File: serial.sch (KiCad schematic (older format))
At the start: 53 parts, among them CN304 Conn_02x13_Odd_Even, CN305 DB25P, CN306 Conn_01x03_Male, Q300 2SC945, Q302 2N3906, U1 PST518B, U301 8520, U302 74LS32, U303 74F08, U304 1488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

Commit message: Associate footprints with components
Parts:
- CN304: footprint (none) -> Connector_PinSocket_2.54mm:PinSocket_2x13_P2.54mm_Vertical
- CN305: footprint (none) -> Connector_Dsub:DSUB-25_Male_Horizontal_P2.77x2.84mm_EdgePinOffset7.70mm_Housed_MountingHolesOffset9.12mm
- CN306, EMI325, EMI326, EMI327, EMI328, EMI329, EMI330, EMI331, EMI332, EMI333, EMI334: footprint (none) -> Connector_PinSocket_2.54mm:PinSocket_1x03_P2.54mm_Vertical
- F2: footprint (none) -> Fuse:Fuse_Littelfuse-LVR100
- Q300: footprint (none) -> Package_TO_SOT_THT:TO-92_Inline
- R302, R305, R306, R307, R308, R802, R805, R902: footprint (none) -> Resistor_THT:R_Axial_DIN0207_L6.3mm_D2.5mm_P10.16mm_Horizontal
- U1: footprint (none) -> Package_TO_SOT_THT:TO-92L_Inline
- U301: footprint (none) -> Package_DIP:DIP-40_W15.24mm_Socket
- U302, U303, U304, U305, U805: footprint (none) -> Package_DIP:DIP-14_W7.62mm_Socket
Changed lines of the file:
@@
 F 0 "U301" H 2800 4565 50  0000 C CNN
 F 1 "8520" H 2800 4474 50  0000 C CNN
-F 2 "" H 4400 4350 50  0001 C CNN
+F 2 "Package_DIP:DIP-40_W15.24mm_Socket" H 4400 4350 50  0001 C CNN
 F 3 "https://www.amigawiki.org/doku.php?id=de:parts:cia" H 4400 4350 50  0001 C CNN
 	1    2800 4400
@@
 F 0 "U302" H 1650 6183 50  0000 C CNN
 F 1 "74LS32" H 1650 6274 50  0000 C CNN
-F 2 "" H 1650 6500 50  0001 C CNN
+F 2 "Package_DIP:DIP-14_W7.62mm_Socket" H 1650 6500 50  0001 C CNN
 F 3 "http://www.ti.com/lit/gpn/sn74LS32" H 1650 6500 50  0001 C CNN
 	2    1650 6500
@@
 F 0 "U805" H 2150 1083 50  0000 C CNN
 F 1 "LM339" H 2150 1174 50  0000 C CNN
-F 2 "" H 2100 1550 50  0001 C CNN
+F 2 "Package_DIP:DIP-14_W7.62mm_Socket" H 2100 1550 50  0001 C CNN
 F 3 "http://www.ti.com/lit/ds/symlink/lm339.pdf" H 2200 1650 50  0001 C CNN
 	2    2150 1450
@@
 F 0 "R802" H 2670 1246 50  0000 L CNN
 F 1 "10k" H 2670 1155 50  0000 L CNN
-F 2 "" V 2530 1200 50  0001 C CNN
+F 2 "Resistor_THT:R_Axial_DIN0207_L6.3mm_D2.5mm_P10.16mm_Horizontal" V 2530 1200 50  0001 C CNN
 F 3 "~" H 2600 1200 50  0001 C CNN
 	1    2600 1200
@@
 F 0 "U805" H 3800 1183 50  0000 C CNN
 F 1 "LM339" H 3800 1274 50  0000 C CNN
-F 2 "" H 3750 1650 50  0001 C CNN
+F 2 "Package_DIP:DIP-14_W7.62mm_Socket" H 3750 1650 50  0001 C CNN
 F 3 "http://www.ti.com/lit/ds/symlink/lm339.pdf" H 3850 1750 50  0001 C CNN
 	1    3800 1550
@@
 F 0 "U805" H 5250 1283 50  0000 C CNN
 F 1 "LM339" H 5250 1374 50  0000 C CNN
-F 2 "" H 5200 1750 50  0001 C CNN
+F 2 "Package_DIP:DIP-14_W7.62mm_Socket" H 5200 1750 50  0001 C CNN
 F 3 "http://www.ti.com/lit/ds/symlink/lm339.pdf" H 5300 1850 50  0001 C CNN
 	3    5250 1650
@@
 F 0 "U805" H 6700 1383 50  0000 C CNN
 F 1 "LM339" H 6700 1474 50  0000 C CNN
-F 2 "" H 6650 1850 50  0001 C CNN
+F 2 "Package_DIP:DIP-14_W7.62mm_Socket" H 6650 1850 50  0001 C CNN
 F 3 "http://www.ti.com/lit/ds/symlink/lm339.pdf" H 6750 1950 50  0001 C CNN
 	4    6700 1750
@@
 F 0 "U805" H 762 2254 50  0000 R CNN
 F 1 "LM339" H 762 2345 50  0000 R CNN
-F 2 "" H 900 2400 50  0001 C CNN
+F 2 "Package_DIP:DIP-14_W7.62mm_Socket" H 900 2400 50  0001 C CNN
 F 3 "http://www.ti.com/lit/ds/symlink/lm339.pdf" H 1000 2500 50  0001 C CNN
 	5    950  2300
@@
 F 0 "R805" H 4320 1446 50  0000 L CNN
 F 1 "47k" H 4320 1355 50  0000 L CNN
-F 2 "" V 4180 1400 50  0001 C CNN
+F 2 "Resistor_THT:R_Axial_DIN0207_L6.3mm_D2.5mm_P10.16mm_Horizontal" V 4180 1400 50  0001 C CNN
 F 3 "~" H 4250 1400 50  0001 C CNN
 	1    4250 1400
@@
 F 0 "CN305" H 14830 6696 50  0000 L CNN
 F 1 "DB25P" H 14830 6605 50  0000 L CNN
-F 2 "" H 14650 6650 50  0001 C CNN
+F 2 "Connector_Dsub:DSUB-25_Male_Horizontal_P2.77x2.84mm_EdgePinOffset7.70mm_Housed_MountingHolesOffset9.12mm" H 14650 6650 50  0001 C CNN
 F 3 " ~" H 14650 6650 50  0001 C CNN
 F 4 "Male" H 14650 6650 50  0001 C CNN "Gender"
@@
 F 0 "R307" H 8770 2746 50  0000 L CNN
 F 1 "68" H 8770 2655 50  0000 L CNN
-F 2 "" V 8630 2700 50  0001 C CNN
+F 2 "Resistor_THT:R_Axial_DIN0207_L6.3mm_D2.5mm_P10.16mm_Horizontal" V 8630 2700 50  0001 C CNN
 F 3 "~" H 8700 2700 50  0001 C CNN
 	1    8700 2700
@@
 F 0 "R902" H 7920 2696 50  0000 L CNN
 F 1 "4.7k" H 7920 2605 50  0000 L CNN
-F 2 "" V 7780 2650 50  0001 C CNN
+F 2 "Resistor_THT:R_Axial_DIN0207_L6.3mm_D2.5mm_P10.16mm_Horizontal" V 7780 2650 50  0001 C CNN
 F 3 "~" H 7850 2650 50  0001 C CNN
 	1    7850 2650
@@
 F 0 "CN306" H 10272 2678 50  0000 R CNN
 F 1 "Conn_01x03_Male" H 10408 2890 50  0001 C CNN
-F 2 "" H 10300 2700 50  0001 C CNN
+F 2 "Connector_PinSocket_2.54mm:PinSocket_1x03_P2.54mm_Vertical" H 10300 2700 50  0001 C CNN
 F 3 "~" H 10300 2700 50  0001 C CNN
 	1    10300 2700
@@
 F 0 "CN304" V 11100 3512 50  0000 R CNN
 F 1 "Conn_02x13_Odd_Even" V 11055 3512 50  0001 R CNN
-F 2 "" H 11050 4200 50  0001 C CNN
+F 2 "Connector_PinSocket_2.54mm:PinSocket_2x13_P2.54mm_Vertical" H 11050 4200 50  0001 C CNN
 F 3 "~" H 11050 4200 50  0001 C CNN
 F 4 "Male" V 11050 4200 50  0001 C CNN "Gender"
@@
 F 0 "U303" H 6250 3775 50  0000 C CNN
 F 1 "74F08" H 6250 3684 50  0000 C CNN
-F 2 "" H 6250 3450 50  0001 C CNN
+F 2 "Package_DIP:DIP-14_W7.62mm_Socket" H 6250 3450 50  0001 C CNN
 F 3 "http://www.ti.com/lit/gpn/sn74LS08" H 6250 3450 50  0001 C CNN
 	2    6250 3450
@@
 F 0 "EMI326" H 11600 5663 50  0000 C CNN
 F 1 "C_Feedthrough" H 11600 5664 50  0001 C CNN
-F 2 "" V 11600 5450 50  0001 C CNN
+F 2 "Connector_PinSocket_2.54mm:PinSocket_1x03_P2.54mm_Vertical" V 11600 5450 50  0001 C CNN
 F 3 "~" V 11600 5450 50  0001 C CNN
 	1    11600 5450
@@
 F 0 "EMI327" H 11600 6063 50  0000 C CNN
 F 1 "C_Feedthrough" H 11600 6064 50  0001 C CNN
-F 2 "" V 11600 5850 50  0001 C CNN
+F 2 "Connector_PinSocket_2.54mm:PinSocket_1x03_P2.54mm_Vertical" V 11600 5850 50  0001 C CNN
 F 3 "~" V 11600 5850 50  0001 C CNN
 	1    11600 5850
@@
 F 0 "EMI330" H 11600 7513 50  0000 C CNN
 F 1 "C_Feedthrough" H 11600 7514 50  0001 C CNN
-F 2 "" V 11600 7300 50  0001 C CNN
+F 2 "Connector_PinSocket_2.54mm:PinSocket_1x03_P2.54mm_Vertical" V 11600 7300 50  0001 C CNN
 F 3 "~" V 11600 7300 50  0001 C CNN
 	1    11600 7300
@@
 F 0 "EMI334" H 15200 8613 50  0000 C CNN
 F 1 "C_Feedthrough" H 15200 8614 50  0001 C CNN
-F 2 "" V 15200 8400 50  0001 C CNN
+F 2 "Connector_PinSocket_2.54mm:PinSocket_1x03_P2.54mm_Vertical" V 15200 8400 50  0001 C CNN
 F 3 "~" V 15200 8400 50  0001 C CNN
 	1    15200 8400
@@
 F 0 "EMI333" H 12950 8713 50  0000 C CNN
 F 1 "C_Feedthrough" H 12950 8714 50  0001 C CNN
-F 2 "" V 12950 8500 50  0001 C CNN
+F 2 "Connector_PinSocket_2.54mm:PinSocket_1x03_P2.54mm_Vertical" V 12950 8500 50  0001 C CNN
 F 3 "~" V 12950 8500 50  0001 C CNN
 	1    12950 8500
@@
 F 0 "EMI332" H 14600 8613 50  0000 C CNN
 F 1 "C_Feedthrough" H 14600 8614 50  0001 C CNN
-F 2 "" V 14600 8400 50  0001 C CNN
+F 2 "Connector_PinSocket_2.54mm:PinSocket_1x03_P2.54mm_Vertical" V 14600 8400 50  0001 C CNN
 F 3 "~" V 14600 8400 50  0001 C CNN
 	1    14600 8400
@@
 F 0 "EMI331" H 11600 8063 50  0000 C CNN
 F 1 "C_Feedthrough" H 11600 8064 50  0001 C CNN
-F 2 "" V 11600 7850 50  0001 C CNN
+F 2 "Connector_PinSocket_2.54mm:PinSocket_1x03_P2.54mm_Vertical" V 11600 7850 50  0001 C CNN
 F 3 "~" V 11600 7850 50  0001 C CNN
 	1    11600 7850
@@
 F 0 "EMI325" H 11600 5263 50  0000 C CNN
 F 1 "C_Feedthrough" H 11600 5264 50  0001 C CNN
-F 2 "" V 11600 5050 50  0001 C CNN
+F 2 "Connector_PinSocket_2.54mm:PinSocket_1x03_P2.54mm_Vertical" V 11600 5050 50  0001 C CNN
 F 3 "~" V 11600 5050 50  0001 C CNN
 	1    11600 5050
@@
 F 0 "EMI329" H 11600 7113 50  0000 C CNN
 F 1 "C_Feedthrough" H 11600 7114 50  0001 C CNN
-F 2 "" V 11600 6900 50  0001 C CNN
+F 2 "Connector_PinSocket_2.54mm:PinSocket_1x03_P2.54mm_Vertical" V 11600 6900 50  0001 C CNN
 F 3 "~" V 11600 6900 50  0001 C CNN
 	1    11600 6900
@@
 F 0 "EMI328" H 11600 6713 50  0000 C CNN
 F 1 "C_Feedthrough" H 11600 6714 50  0001 C CNN
-F 2 "" V 11600 6500 50  0001 C CNN
+F 2 "Connector_PinSocket_2.54mm:PinSocket_1x03_P2.54mm_Vertical" V 11600 6500 50  0001 C CNN
 F 3 "~" V 11600 6500 50  0001 C CNN
 	1    11600 6500
@@
 F 0 "R308" H 9220 2496 50  0000 L CNN
 F 1 "200" H 9220 2405 50  0000 L CNN
-F 2 "" V 9080 2450 50  0001 C CNN
+F 2 "Resistor_THT:R_Axial_DIN0207_L6.3mm_D2.5mm_P10.16mm_Horizontal" V 9080 2450 50  0001 C CNN
 F 3 "~" H 9150 2450 50  0001 C CNN
 	1    9150 2450
@@
 F 0 "U304" H 6450 4525 50  0000 C CNN
 F 1 "1488" H 6450 4434 50  0000 C CNN
-F 2 "" H 6450 4500 50  0001 C CNN
+F 2 "Package_DIP:DIP-14_W7.62mm_Socket" H 6450 4500 50  0001 C CNN
 F 3 "https://www.onsemi.com/pub/Collateral/MC1488-D.PDF" H 6450 4500 50  0001 C CNN
 	1    6450 4500
@@
 F 0 "U305" H 6450 6225 50  0000 C CNN
 F 1 "1489" H 6450 6134 50  0000 C CNN
-F 2 "" H 6450 6200 50  0001 C CNN
+F 2 "Package_DIP:DIP-14_W7.62mm_Socket" H 6450 6200 50  0001 C CNN
 F 3 "https://www.onsemi.com/pub/Collateral/MC1489-D.PDF" H 6450 6200 50  0001 C CNN
 	1    6450 6200
@@
 F 0 "Q300" H 10641 8846 50  0000 L CNN
 F 1 "2SC945" H 10641 8755 50  0000 L CNN
-F 2 "" H 10650 8900 50  0001 C CNN
+F 2 "Package_TO_SOT_THT:TO-92_Inline" H 10650 8900 50  0001 C CNN
 F 3 "~" H 10450 8800 50  0001 C CNN
 	1    10450 8800
@@
 F 0 "R305" H 10970 9096 50  0000 L CNN
 F 1 "10k" H 10970 9005 50  0000 L CNN
-F 2 "" V 10830 9050 50  0001 C CNN
+F 2 "Resistor_THT:R_Axial_DIN0207_L6.3mm_D2.5mm_P10.16mm_Horizontal" V 10830 9050 50  0001 C CNN
 F 3 "~" H 10900 9050 50  0001 C CNN
 	1    10900 9050
@@
 F 0 "R306" H 11420 8596 50  0000 L CNN
 F 1 "10k" H 11420 8505 50  0000 L CNN
-F 2 "" V 11280 8550 50  0001 C CNN
+F 2 "Resistor_THT:R_Axial_DIN0207_L6.3mm_D2.5mm_P10.16mm_Horizontal" V 11280 8550 50  0001 C CNN
 F 3 "~" H 11350 8550 50  0001 C CNN
 	1    11350 8550
@@
 F 0 "R302" V 13193 9050 50  0000 C CNN
 F 1 "1k" V 13284 9050 50  0000 C CNN
-F 2 "" V 13330 9050 50  0001 C CNN
+F 2 "Resistor_THT:R_Axial_DIN0207_L6.3mm_D2.5mm_P10.16mm_Horizontal" V 13330 9050 50  0001 C CNN
 F 3 "~" H 13400 9050 50  0001 C CNN
 	1    13400 9050
@@
 F 0 "F2" H 14910 8900 50  0000 L CNN
 F 1 "Fuse" H 14910 8855 50  0001 L CNN
-F 2 "" V 14780 8900 50  0001 C CNN
+F 2 "Fuse:Fuse_Littelfuse-LVR100" V 14780 8900 50  0001 C CNN
 F 3 "~" H 14850 8900 50  0001 C CNN
 	1    14850 8900
@@
 F 0 "U1" H 3475 765 50  0000 C CNN
 F 1 "PST518B" H 3475 674 50  0000 C CNN
-F 2 "" H 3400 650 50  0001 C CNN
+F 2 "Package_TO_SOT_THT:TO-92L_Inline" H 3400 650 50  0001 C CNN
 F 3 "http://www.amigawiki.org/lib/exe/fetch.php?media=de:service:upgrades:pst518b_mitsumi_datasheet.pdf" H 3400 650 50  0001 C CNN
 	1    3400 650

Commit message: Associate more components
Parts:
- C317, C318, C813, C814: footprint (none) -> Capacitor_THT:CP_Radial_D8.0mm_P5.00mm
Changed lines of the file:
@@
 F 0 "C813" H 2718 1746 50  0000 L CNN
 F 1 "22uF 16V" H 2718 1655 50  0000 L CNN
-F 2 "" H 2638 1550 50  0001 C CNN
+F 2 "Capacitor_THT:CP_Radial_D8.0mm_P5.00mm" H 2638 1550 50  0001 C CNN
 F 3 "~" H 2600 1700 50  0001 C CNN
 	1    2600 1700
@@
 F 0 "C814" H 4368 1746 50  0000 L CNN
 F 1 "22uF 16V" H 4368 1655 50  0000 L CNN
-F 2 "" H 4288 1550 50  0001 C CNN
+F 2 "Capacitor_THT:CP_Radial_D8.0mm_P5.00mm" H 4288 1550 50  0001 C CNN
 F 3 "~" H 4250 1700 50  0001 C CNN
 	1    4250 1700
@@
 F 0 "C318" H 12668 8946 50  0000 L CNN
 F 1 "22uF 16V" H 12668 8855 50  0000 L CNN
-F 2 "" H 12588 8750 50  0001 C CNN
+F 2 "Capacitor_THT:CP_Radial_D8.0mm_P5.00mm" H 12588 8750 50  0001 C CNN
 F 3 "~" H 12550 8900 50  0001 C CNN
 	1    12550 8900
@@
 F 0 "C317" H 13268 4996 50  0000 L CNN
 F 1 "22uF 16V" H 13268 4905 50  0000 L CNN
-F 2 "" H 13188 4800 50  0001 C CNN
+F 2 "Capacitor_THT:CP_Radial_D8.0mm_P5.00mm" H 13188 4800 50  0001 C CNN
 F 3 "~" H 13150 4950 50  0001 C CNN
 	1    13150 4950

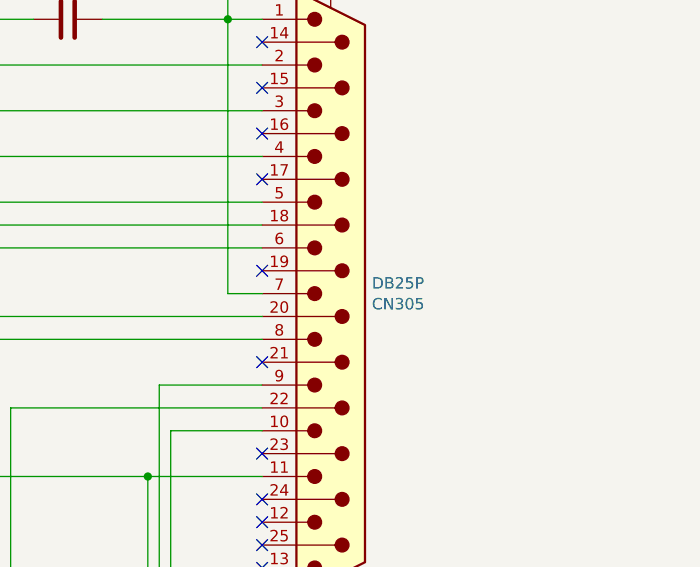
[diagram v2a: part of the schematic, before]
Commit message: Change namings
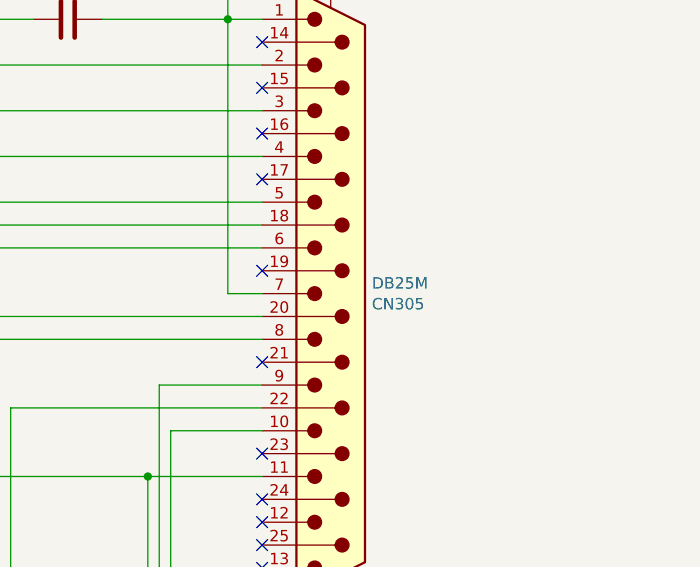
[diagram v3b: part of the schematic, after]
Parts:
- CN305: value DB25P -> DB25M
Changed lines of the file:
@@
 P 14650 6650
 F 0 "CN305" H 14830 6696 50  0000 L CNN
-F 1 "DB25P" H 14830 6605 50  0000 L CNN
+F 1 "DB25M" H 14830 6605 50  0000 L CNN
 F 2 "Connector_Dsub:DSUB-25_Male_Horizontal_P2.77x2.84mm_EdgePinOffset7.70mm_Housed_MountingHolesOffset9.12mm" H 14650 6650 50  0001 C CNN
 F 3 " ~" H 14650 6650 50  0001 C CNN

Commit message: Update footprints
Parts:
- C301, C304, C305, C306, C310, C311, C312, C313, C314, C315, C316, C320, C321, C805, C815, C919: footprint (none) -> Capacitor_THT:C_Rect_L11.0mm_W2.8mm_P10.00mm_MKT
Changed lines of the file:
@@
 F 0 "C301" H 1715 4496 50  0000 L CNN
 F 1 "0.1uF" H 1715 4405 50  0000 L CNN
-F 2 "" H 1638 4300 50  0001 C CNN
+F 2 "Capacitor_THT:C_Rect_L11.0mm_W2.8mm_P10.00mm_MKT" H 1638 4300 50  0001 C CNN
 F 3 "~" H 1600 4450 50  0001 C CNN
 	1    1600 4450
@@
 F 0 "C805" H 1165 2346 50  0000 L CNN
 F 1 "0.1uF" H 1165 2255 50  0000 L CNN
-F 2 "" H 1088 2150 50  0001 C CNN
+F 2 "Capacitor_THT:C_Rect_L11.0mm_W2.8mm_P10.00mm_MKT" H 1088 2150 50  0001 C CNN
 F 3 "~" H 1050 2300 50  0001 C CNN
 	1    1050 2300
@@
 F 0 "C815" H 4165 2296 50  0000 L CNN
 F 1 "0.1uF" H 4165 2205 50  0000 L CNN
-F 2 "" H 4088 2100 50  0001 C CNN
+F 2 "Capacitor_THT:C_Rect_L11.0mm_W2.8mm_P10.00mm_MKT" H 4088 2100 50  0001 C CNN
 F 3 "~" H 4050 2250 50  0001 C CNN
 	1    4050 2250
@@
 F 0 "C320" H 10115 4196 50  0000 L CNN
 F 1 "470pF" H 10115 4105 50  0000 L CNN
-F 2 "" H 10038 4000 50  0001 C CNN
+F 2 "Capacitor_THT:C_Rect_L11.0mm_W2.8mm_P10.00mm_MKT" H 10038 4000 50  0001 C CNN
 F 3 "~" H 10000 4150 50  0001 C CNN
 	1    10000 4150
@@
 F 0 "C321" V 11348 3350 50  0000 C CNN
 F 1 "470pF" V 11439 3350 50  0000 C CNN
-F 2 "" H 11638 3200 50  0001 C CNN
+F 2 "Capacitor_THT:C_Rect_L11.0mm_W2.8mm_P10.00mm_MKT" H 11638 3200 50  0001 C CNN
 F 3 "~" H 11600 3350 50  0001 C CNN
 	1    11600 3350
@@
 F 0 "C919" H 9265 2996 50  0000 L CNN
 F 1 "0.1uF" H 9265 2905 50  0000 L CNN
-F 2 "" H 9188 2800 50  0001 C CNN
+F 2 "Capacitor_THT:C_Rect_L11.0mm_W2.8mm_P10.00mm_MKT" H 9188 2800 50  0001 C CNN
 F 3 "~" H 9150 2950 50  0001 C CNN
 	1    9150 2950
@@
 F 0 "C305" V 6198 7850 50  0000 C CNN
 F 1 "0.01uF" V 6289 7850 50  0000 C CNN
-F 2 "" H 6488 7700 50  0001 C CNN
+F 2 "Capacitor_THT:C_Rect_L11.0mm_W2.8mm_P10.00mm_MKT" H 6488 7700 50  0001 C CNN
 F 3 "~" H 6450 7850 50  0001 C CNN
 	1    6450 7850
@@
 F 0 "C314" H 7565 4346 50  0000 L CNN
 F 1 "1000pF" H 7565 4255 50  0000 L CNN
-F 2 "" H 7488 4150 50  0001 C CNN
+F 2 "Capacitor_THT:C_Rect_L11.0mm_W2.8mm_P10.00mm_MKT" H 7488 4150 50  0001 C CNN
 F 3 "~" H 7450 4300 50  0001 C CNN
 	1    7450 4300
@@
 F 0 "C315" H 8015 4646 50  0000 L CNN
 F 1 "1000pF" H 8015 4555 50  0000 L CNN
-F 2 "" H 7938 4450 50  0001 C CNN
+F 2 "Capacitor_THT:C_Rect_L11.0mm_W2.8mm_P10.00mm_MKT" H 7938 4450 50  0001 C CNN
 F 3 "~" H 7900 4600 50  0001 C CNN
 	1    7900 4600
@@
 F 0 "C316" H 8415 4346 50  0000 L CNN
 F 1 "1000pF" H 8415 4255 50  0000 L CNN
-F 2 "" H 8338 4150 50  0001 C CNN
+F 2 "Capacitor_THT:C_Rect_L11.0mm_W2.8mm_P10.00mm_MKT" H 8338 4150 50  0001 C CNN
 F 3 "~" H 8300 4300 50  0001 C CNN
 	1    8300 4300
@@
 F 0 "C310" H 7615 8146 50  0000 L CNN
 F 1 "1000pF" H 7615 8055 50  0000 L CNN
-F 2 "" H 7538 7950 50  0001 C CNN
+F 2 "Capacitor_THT:C_Rect_L11.0mm_W2.8mm_P10.00mm_MKT" H 7538 7950 50  0001 C CNN
 F 3 "~" H 7500 8100 50  0001 C CNN
 	1    7500 8100
@@
 F 0 "C311" H 8115 8146 50  0000 L CNN
 F 1 "1000pF" H 8115 8055 50  0000 L CNN
-F 2 "" H 8038 7950 50  0001 C CNN
+F 2 "Capacitor_THT:C_Rect_L11.0mm_W2.8mm_P10.00mm_MKT" H 8038 7950 50  0001 C CNN
 F 3 "~" H 8000 8100 50  0001 C CNN
 	1    8000 8100
@@
 F 0 "C312" H 8615 8146 50  0000 L CNN
 F 1 "1000pF" H 8615 8055 50  0000 L CNN
-F 2 "" H 8538 7950 50  0001 C CNN
+F 2 "Capacitor_THT:C_Rect_L11.0mm_W2.8mm_P10.00mm_MKT" H 8538 7950 50  0001 C CNN
 F 3 "~" H 8500 8100 50  0001 C CNN
 	1    8500 8100
@@
 F 0 "C313" H 9115 8146 50  0000 L CNN
 F 1 "1000pF" H 9115 8055 50  0000 L CNN
-F 2 "" H 9038 7950 50  0001 C CNN
+F 2 "Capacitor_THT:C_Rect_L11.0mm_W2.8mm_P10.00mm_MKT" H 9038 7950 50  0001 C CNN
 F 3 "~" H 9000 8100 50  0001 C CNN
 	1    9000 8100
@@
 F 0 "C304" H 13965 8396 50  0000 L CNN
 F 1 "100pF" H 13965 8305 50  0000 L CNN
-F 2 "" H 13888 8200 50  0001 C CNN
+F 2 "Capacitor_THT:C_Rect_L11.0mm_W2.8mm_P10.00mm_MKT" H 13888 8200 50  0001 C CNN
 F 3 "~" H 13850 8350 50  0001 C CNN
 	1    13850 8350
@@
 F 0 "C306" V 13248 5450 50  0000 C CNN
 F 1 "100pF" V 13339 5450 50  0000 C CNN
-F 2 "" H 13538 5300 50  0001 C CNN
+F 2 "Capacitor_THT:C_Rect_L11.0mm_W2.8mm_P10.00mm_MKT" H 13538 5300 50  0001 C CNN
 F 3 "~" H 13500 5450 50  0001 C CNN
 	1    13500 5450

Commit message: More placement
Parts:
- CN304: footprint Connector_PinSocket_2.54mm:PinSocket_2x13_P2.54mm_Vertical -> Connector_PinHeader_2.54mm:PinHeader_2x13_P2.54mm_Vertical
- CN306: footprint Connector_PinSocket_2.54mm:PinSocket_1x03_P2.54mm_Vertical -> Connector_PinHeader_2.54mm:PinHeader_1x03_P2.54mm_Vertical
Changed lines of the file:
@@
 F 0 "CN306" H 10272 2678 50  0000 R CNN
 F 1 "Conn_01x03_Male" H 10408 2890 50  0001 C CNN
-F 2 "Connector_PinSocket_2.54mm:PinSocket_1x03_P2.54mm_Vertical" H 10300 2700 50  0001 C CNN
+F 2 "Connector_PinHeader_2.54mm:PinHeader_1x03_P2.54mm_Vertical" H 10300 2700 50  0001 C CNN
 F 3 "~" H 10300 2700 50  0001 C CNN
 	1    10300 2700
@@
 F 0 "CN304" V 11100 3512 50  0000 R CNN
 F 1 "Conn_02x13_Odd_Even" V 11055 3512 50  0001 R CNN
-F 2 "Connector_PinSocket_2.54mm:PinSocket_2x13_P2.54mm_Vertical" H 11050 4200 50  0001 C CNN
+F 2 "Connector_PinHeader_2.54mm:PinHeader_2x13_P2.54mm_Vertical" H 11050 4200 50  0001 C CNN
 F 3 "~" H 11050 4200 50  0001 C CNN
 F 4 "Male" V 11050 4200 50  0001 C CNN "Gender"

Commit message: first placement pass is done
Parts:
- C310, C311, C312, C313, C314, C315, C316, C320, C321: footprint Capacitor_THT:C_Rect_L11.0mm_W2.8mm_P10.00mm_MKT -> Capacitor_THT:C_Rect_L7.0mm_W2.0mm_P5.00mm
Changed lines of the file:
@@
 F 0 "C320" H 10115 4196 50  0000 L CNN
 F 1 "470pF" H 10115 4105 50  0000 L CNN
-F 2 "Capacitor_THT:C_Rect_L11.0mm_W2.8mm_P10.00mm_MKT" H 10038 4000 50  0001 C CNN
+F 2 "Capacitor_THT:C_Rect_L7.0mm_W2.0mm_P5.00mm" H 10038 4000 50  0001 C CNN
 F 3 "~" H 10000 4150 50  0001 C CNN
 	1    10000 4150
@@
 F 0 "C321" V 11348 3350 50  0000 C CNN
 F 1 "470pF" V 11439 3350 50  0000 C CNN
-F 2 "Capacitor_THT:C_Rect_L11.0mm_W2.8mm_P10.00mm_MKT" H 11638 3200 50  0001 C CNN
+F 2 "Capacitor_THT:C_Rect_L7.0mm_W2.0mm_P5.00mm" H 11638 3200 50  0001 C CNN
 F 3 "~" H 11600 3350 50  0001 C CNN
 	1    11600 3350
@@
 F 0 "C314" H 7565 4346 50  0000 L CNN
 F 1 "1000pF" H 7565 4255 50  0000 L CNN
-F 2 "Capacitor_THT:C_Rect_L11.0mm_W2.8mm_P10.00mm_MKT" H 7488 4150 50  0001 C CNN
+F 2 "Capacitor_THT:C_Rect_L7.0mm_W2.0mm_P5.00mm" H 7488 4150 50  0001 C CNN
 F 3 "~" H 7450 4300 50  0001 C CNN
 	1    7450 4300
@@
 F 0 "C315" H 8015 4646 50  0000 L CNN
 F 1 "1000pF" H 8015 4555 50  0000 L CNN
-F 2 "Capacitor_THT:C_Rect_L11.0mm_W2.8mm_P10.00mm_MKT" H 7938 4450 50  0001 C CNN
+F 2 "Capacitor_THT:C_Rect_L7.0mm_W2.0mm_P5.00mm" H 7938 4450 50  0001 C CNN
 F 3 "~" H 7900 4600 50  0001 C CNN
 	1    7900 4600
@@
 F 0 "C316" H 8415 4346 50  0000 L CNN
 F 1 "1000pF" H 8415 4255 50  0000 L CNN
-F 2 "Capacitor_THT:C_Rect_L11.0mm_W2.8mm_P10.00mm_MKT" H 8338 4150 50  0001 C CNN
+F 2 "Capacitor_THT:C_Rect_L7.0mm_W2.0mm_P5.00mm" H 8338 4150 50  0001 C CNN
 F 3 "~" H 8300 4300 50  0001 C CNN
 	1    8300 4300
@@
 F 0 "C310" H 7615 8146 50  0000 L CNN
 F 1 "1000pF" H 7615 8055 50  0000 L CNN
-F 2 "Capacitor_THT:C_Rect_L11.0mm_W2.8mm_P10.00mm_MKT" H 7538 7950 50  0001 C CNN
+F 2 "Capacitor_THT:C_Rect_L7.0mm_W2.0mm_P5.00mm" H 7538 7950 50  0001 C CNN
 F 3 "~" H 7500 8100 50  0001 C CNN
 	1    7500 8100
@@
 F 0 "C311" H 8115 8146 50  0000 L CNN
 F 1 "1000pF" H 8115 8055 50  0000 L CNN
-F 2 "Capacitor_THT:C_Rect_L11.0mm_W2.8mm_P10.00mm_MKT" H 8038 7950 50  0001 C CNN
+F 2 "Capacitor_THT:C_Rect_L7.0mm_W2.0mm_P5.00mm" H 8038 7950 50  0001 C CNN
 F 3 "~" H 8000 8100 50  0001 C CNN
 	1    8000 8100
@@
 F 0 "C312" H 8615 8146 50  0000 L CNN
 F 1 "1000pF" H 8615 8055 50  0000 L CNN
-F 2 "Capacitor_THT:C_Rect_L11.0mm_W2.8mm_P10.00mm_MKT" H 8538 7950 50  0001 C CNN
+F 2 "Capacitor_THT:C_Rect_L7.0mm_W2.0mm_P5.00mm" H 8538 7950 50  0001 C CNN
 F 3 "~" H 8500 8100 50  0001 C CNN
 	1    8500 8100
@@
 F 0 "C313" H 9115 8146 50  0000 L CNN
 F 1 "1000pF" H 9115 8055 50  0000 L CNN
-F 2 "Capacitor_THT:C_Rect_L11.0mm_W2.8mm_P10.00mm_MKT" H 9038 7950 50  0001 C CNN
+F 2 "Capacitor_THT:C_Rect_L7.0mm_W2.0mm_P5.00mm" H 9038 7950 50  0001 C CNN
 F 3 "~" H 9000 8100 50  0001 C CNN
 	1    9000 8100
